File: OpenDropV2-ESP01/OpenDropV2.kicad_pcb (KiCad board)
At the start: 2 copper layers, 100 x 100 mm, 232 parts, among them J1 DC_JACK, P1 CONN_01X01, P10 CONN_01X01, P11 CONN_01X01, P12 CONN_01X01, P13 ScrewPad1, P14 ScrewPad2, P15 ScrewPad3, P16 ScrewPad4, P2 CONN_01X01, P3 CONN_01X01, P5 CONN_01X01, P6 CONN_01X30, P7 CONN_01X01, P8 CONN_01X01, P9 CONN_01X01, Q1 BSS138, Q2 BSS138, Q3 BSS138, Q5 BSS138, Q6 BSS138, Q7 BSS138, SW1 SW_PUSH, SW2 SW_PUSH, SW5 SPST, T1 IRF 840S, U1 MAX1771ESA, U2 HV507, U3 ARDUINO_MICRO, U4 HV507, U5 ESP8266_SMD, U6 MCP6002

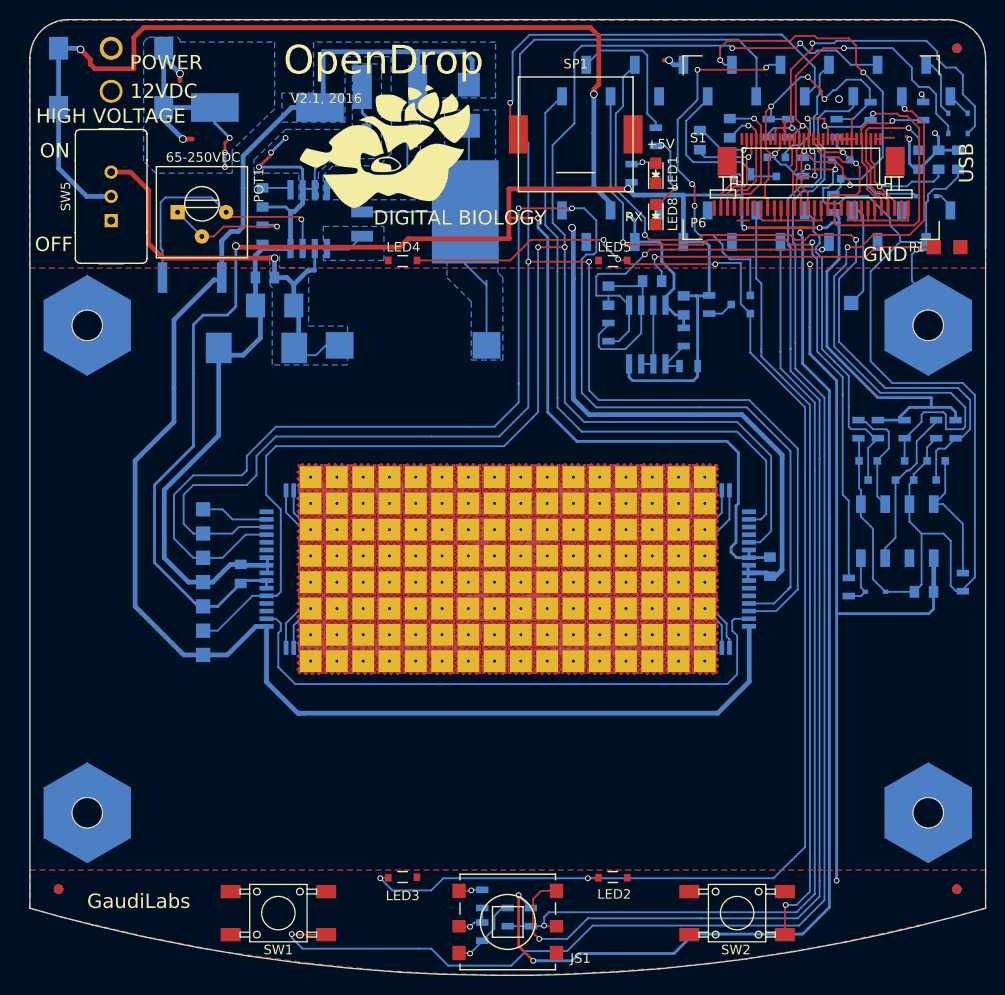
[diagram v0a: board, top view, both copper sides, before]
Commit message: cleaned up folder structure
V2-ESP01 and C2-ESP201
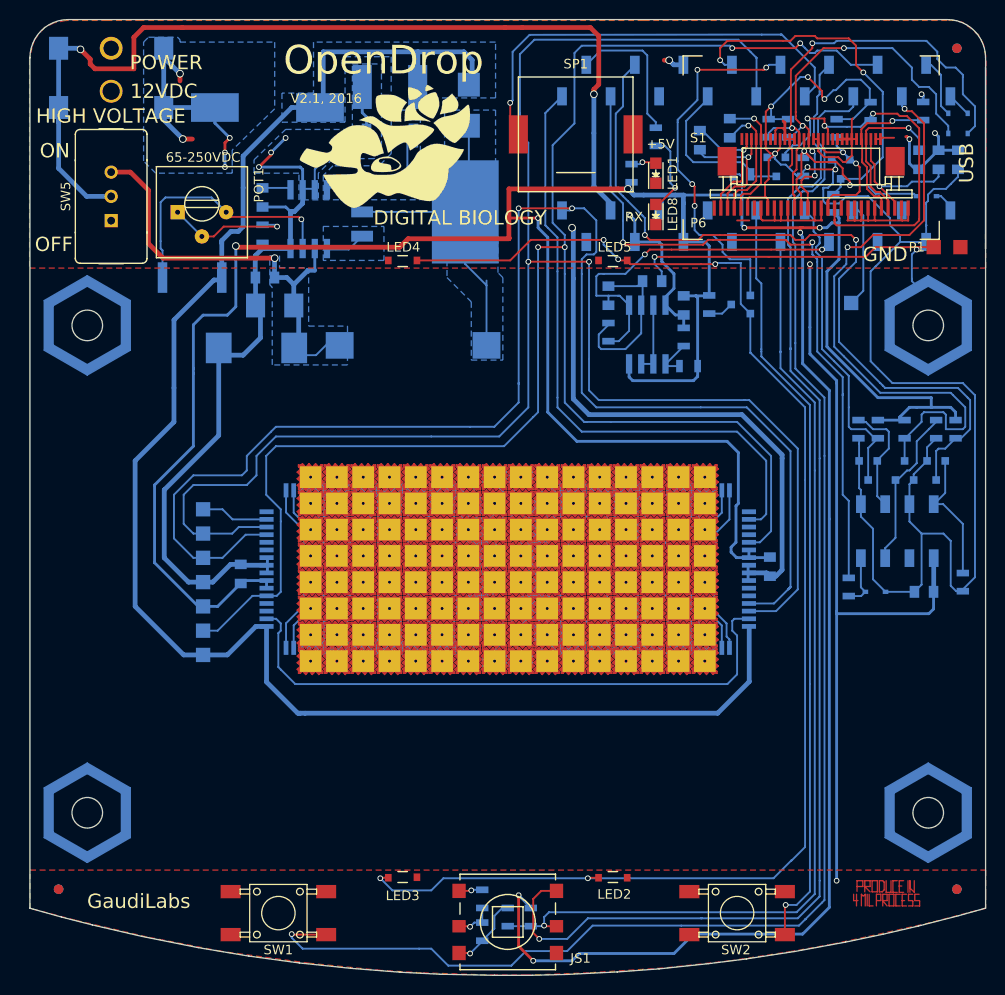
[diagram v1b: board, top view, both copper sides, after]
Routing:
- net (no net): track 1.27 -> 54.7 mm
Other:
- net class 4mil added: clearance 0.1, trace_width 0.1, via_dia 0.6, via_drill 0.4
- rule trace_min: 0.2 -> 0.1

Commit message: Updated Arduino Code to V2.1
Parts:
- removed P14: ScrewPad2, GaudiLabsFootPrints:MountingHolePad_3x9mm
- removed P15: ScrewPad3, GaudiLabsFootPrints:MountingHolePad_3x9mm
- removed P16: ScrewPad4, GaudiLabsFootPrints:MountingHolePad_3x9mm
- added P13: ScrewPad1, GaudiLabsFootPrints:MountingHolePad_3x9mm, F.Cu at (56.0, 74.0)
- added P13: ScrewPad1, GaudiLabsFootPrints:MountingHolePad_3x9mm, F.Cu at (144.0, 125.0)
- added P13: ScrewPad1, GaudiLabsFootPrints:MountingHolePad_3x9mm, F.Cu at (56.0, 125.0)
- C17: value 1uF -> 1pF
- P1, P10, P11, P12, P2, P3, P5, P7, P8, P9: footprint Measurement_Points:Measurement_Point_Square-SMD-Pad_Small -> GaudiLabsFootPrints:Measurement_Point_Square-SMD-Pad_Small
- moved R26 6.06 mm to (145.4, 106.5)
- moved R25 1.58 mm to (143.2, 84.9)
- moved R29 1.36 mm to (145.5, 84.9)
- moved U5 0.96 mm to (139.8, 95.5)
- moved R23 0.53 mm to (141.0, 84.9)
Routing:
- net 3.3V: track 174.8 -> 190.5 mm
- net Net-(Q6-Pad2): track 14.1 -> 20.5 mm
- net (no net): track 54.7 -> 60.2 mm, vias 1 -> 2
- net +5V: track 380.0 -> 378.8 mm
- net ESP_GPIO0: track 64.8 -> 65.9 mm
- net GND: track 345.9 -> 346.8 mm
